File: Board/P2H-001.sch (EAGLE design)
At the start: 29 parts, among them IC1 LTC485N, IC2 74LS07N, IC3 74LS157N, IC4 LTC485N, IC5 TLC5941NT, IC6 TLC5941NT

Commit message: Tuning of routing.
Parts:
- renumbered U$1 to U1
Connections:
- net N$11 renamed LEDA
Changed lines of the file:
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@@
 <part name="SUPPLY18" library="supply2" deviceset="GND" device=""/>
 <part name="SUPPLY17" library="supply2" deviceset="VCC" device=""/>
-<part name="U$1" library="SparkFun-Boards" deviceset="ARDUINO_PRO_MINI" device=""/>
+<part name="U1" library="SparkFun-Boards" deviceset="ARDUINO_PRO_MINI" device=""/>
 </parts>
 <sheets>
@@
 <instance part="SUPPLY18" gate="GND" x="198.12" y="-68.58"/>
 <instance part="SUPPLY17" gate="G$1" x="198.12" y="-33.02"/>
-<instance part="U$1" gate="G$1" x="106.68" y="30.48"/>
+<instance part="U1" gate="G$1" x="106.68" y="30.48"/>
 </instances>
 <busses>
@@
 <wire x1="96.52" y1="38.1" x2="60.96" y2="38.1" width="0.1524" layer="91"/>
 <wire x1="60.96" y1="38.1" x2="60.96" y2="-20.32" width="0.1524" layer="91"/>
-<pinref part="U$1" gate="G$1" pin="GND"/>
+<pinref part="U1" gate="G$1" pin="GND"/>
 </segment>
 <segment>
@@
 <pinref part="SUPPLY11" gate="G$1" pin="VCC"/>
 <wire x1="124.46" y1="38.1" x2="124.46" y2="121.92" width="0.1524" layer="91"/>
-<pinref part="U$1" gate="G$1" pin="VCC"/>
+<pinref part="U1" gate="G$1" pin="VCC"/>
 </segment>
 <segment>
@@
 <wire x1="53.34" y1="45.72" x2="53.34" y2="53.34" width="0.1524" layer="91"/>
 <junction x="53.34" y="53.34"/>
-<pinref part="U$1" gate="G$1" pin="TXO"/>
+<pinref part="U1" gate="G$1" pin="TXO"/>
 </segment>
 </net>
@@
 <label x="86.36" y="22.86" size="1.778" layer="95"/>
 <label x="93.98" y="-7.62" size="1.778" layer="95"/>
-<pinref part="U$1" gate="G$1" pin="7"/>
+<pinref part="U1" gate="G$1" pin="7"/>
 </segment>
 </net>
@@
 <junction x="147.32" y="-10.16"/>
 <label x="93.98" y="-10.16" size="1.778" layer="95"/>
-<pinref part="U$1" gate="G$1" pin="*6"/>
+<pinref part="U1" gate="G$1" pin="*6"/>
 </segment>
 </net>
@@
 <label x="86.36" y="30.48" size="1.778" layer="95"/>
 <label x="93.98" y="-15.24" size="1.778" layer="95"/>
-<pinref part="U$1" gate="G$1" pin="4"/>
+<pinref part="U1" gate="G$1" pin="4"/>
 </segment>
 </net>
@@
 <wire x1="127" y1="-2.54" x2="127" y2="25.4" width="0.1524" layer="91"/>
 <wire x1="127" y1="25.4" x2="119.38" y2="25.4" width="0.1524" layer="91"/>
-<pinref part="U$1" gate="G$1" pin="13"/>
+<pinref part="U1" gate="G$1" pin="13"/>
 </segment>
 </net>
@@
 <wire x1="124.46" y1="-5.08" x2="124.46" y2="20.32" width="0.1524" layer="91"/>
 <wire x1="124.46" y1="20.32" x2="119.38" y2="20.32" width="0.1524" layer="91"/>
-<pinref part="U$1" gate="G$1" pin="*11"/>
+<pinref part="U1" gate="G$1" pin="*11"/>
 </segment>
 </net>
@@
 <pinref part="VDD2" gate="G$1" pin="VDD"/>
 <wire x1="119.38" y1="45.72" x2="119.38" y2="129.54" width="0.1524" layer="91"/>
-<pinref part="U$1" gate="G$1" pin="RAW"/>
+<pinref part="U1" gate="G$1" pin="RAW"/>
 </segment>
 <segment>
@@
 <label x="86.36" y="27.94" size="1.778" layer="95"/>
 <label x="93.98" y="-12.7" size="1.778" layer="95"/>
-<pinref part="U$1" gate="G$1" pin="*5"/>
+<pinref part="U1" gate="G$1" pin="*5"/>
 </segment>
 </net>
@@
 <label x="86.36" y="20.32" size="1.778" layer="95"/>
 <label x="93.98" y="-38.1" size="1.778" layer="95"/>
-<pinref part="U$1" gate="G$1" pin="8"/>
+<pinref part="U1" gate="G$1" pin="8"/>
 </segment>
 </net>
@@
 <wire x1="53.34" y1="-35.56" x2="53.34" y2="43.18" width="0.1524" layer="91"/>
 <wire x1="53.34" y1="43.18" x2="96.52" y2="43.18" width="0.1524" layer="91"/>
-<pinref part="U$1" gate="G$1" pin="RXI"/>
+<pinref part="U1" gate="G$1" pin="RXI"/>
 </segment>
 </net>
@@
 <label x="86.36" y="40.64" size="1.778" layer="95"/>
 <label x="45.72" y="5.08" size="1.778" layer="95"/>
-<pinref part="U$1" gate="G$1" pin="RST"/>
+<pinref part="U1" gate="G$1" pin="RST"/>
 </segment>
 </net>
@@
 <label x="86.36" y="35.56" size="1.778" layer="95"/>
 <label x="45.72" y="15.24" size="1.778" layer="95"/>
-<pinref part="U$1" gate="G$1" pin="2"/>
+<pinref part="U1" gate="G$1" pin="2"/>
 </segment>
 </net>
@@
 <label x="86.36" y="33.02" size="1.778" layer="95"/>
 <label x="45.72" y="2.54" size="1.778" layer="95"/>
-<pinref part="U$1" gate="G$1" pin="*3"/>
+<pinref part="U1" gate="G$1" pin="*3"/>
 </segment>
 </net>
@@
 <pinref part="SV2" gate="1" pin="6"/>
 <label x="93.98" y="0" size="1.778" layer="95"/>
-<pinref part="U$1" gate="G$1" pin="*9"/>
+<pinref part="U1" gate="G$1" pin="*9"/>
 </segment>
 </net>
@@
 <label x="157.48" y="15.24" size="1.778" layer="95"/>
 <label x="175.26" y="33.02" size="1.778" layer="95"/>
-<pinref part="U$1" gate="G$1" pin="A0"/>
+<pinref part="U1" gate="G$1" pin="A0"/>
 </segment>
 </net>
@@
 <pinref part="SV2" gate="1" pin="8"/>
 <label x="147.32" y="33.02" size="1.778" layer="95"/>
-<pinref part="U$1" gate="G$1" pin="A1"/>
+<pinref part="U1" gate="G$1" pin="A1"/>
 </segment>
 </net>
@@
 <label x="157.48" y="10.16" size="1.778" layer="95"/>
 <label x="175.26" y="35.56" size="1.778" layer="95"/>
-<pinref part="U$1" gate="G$1" pin="A2"/>
+<pinref part="U1" gate="G$1" pin="A2"/>
 </segment>
 </net>
@@
 <pinref part="SV2" gate="1" pin="10"/>
 <label x="147.32" y="35.56" size="1.778" layer="95"/>
-<pinref part="U$1" gate="G$1" pin="A3"/>
-</segment>
-</net>
-<net name="N$11" class="0">
+<pinref part="U1" gate="G$1" pin="A3"/>
+</segment>
+</net>
+<net name="LEDA" class="0">
 <segment>
 <pinref part="IC5" gate="G$1" pin="OUT9"/>
@@
 <wire x1="152.4" y1="45.72" x2="121.92" y2="45.72" width="0.1524" layer="91"/>
 <label x="127" y="45.72" size="1.778" layer="95"/>
-<pinref part="U$1" gate="G$1" pin="*10"/>
+<pinref part="U1" gate="G$1" pin="*10"/>
 </segment>
 </net>
@@
 <wire x1="121.92" y1="10.16" x2="121.92" y2="-17.78" width="0.1524" layer="91"/>
 <label x="93.98" y="-17.78" size="1.778" layer="95"/>
-<pinref part="U$1" gate="G$1" pin="A6"/>
+<pinref part="U1" gate="G$1" pin="A6"/>
 </segment>
 </net>
@@
 <label x="157.48" y="2.54" size="1.778" layer="95"/>
 <label x="175.26" y="38.1" size="1.778" layer="95"/>
-<pinref part="U$1" gate="G$1" pin="A4"/>
+<pinref part="U1" gate="G$1" pin="A4"/>
 </segment>
 </net>
@@
 <label x="93.98" y="5.08" size="1.778" layer="95"/>
 <label x="147.32" y="38.1" size="1.778" layer="95"/>
-<pinref part="U$1" gate="G$1" pin="A5"/>
+<pinref part="U1" gate="G$1" pin="A5"/>
 </segment>
 </net>
@@
 <wire x1="193.04" y1="-43.18" x2="205.74" y2="-43.18" width="0.1524" layer="91"/>
 <label x="157.48" y="12.7" size="1.778" layer="95"/>
-<pinref part="U$1" gate="G$1" pin="A7"/>
-</segment>
-</net>
+<pinref part="U1" gate="G$1" pin="A7"/>
+</segment>
+</net>

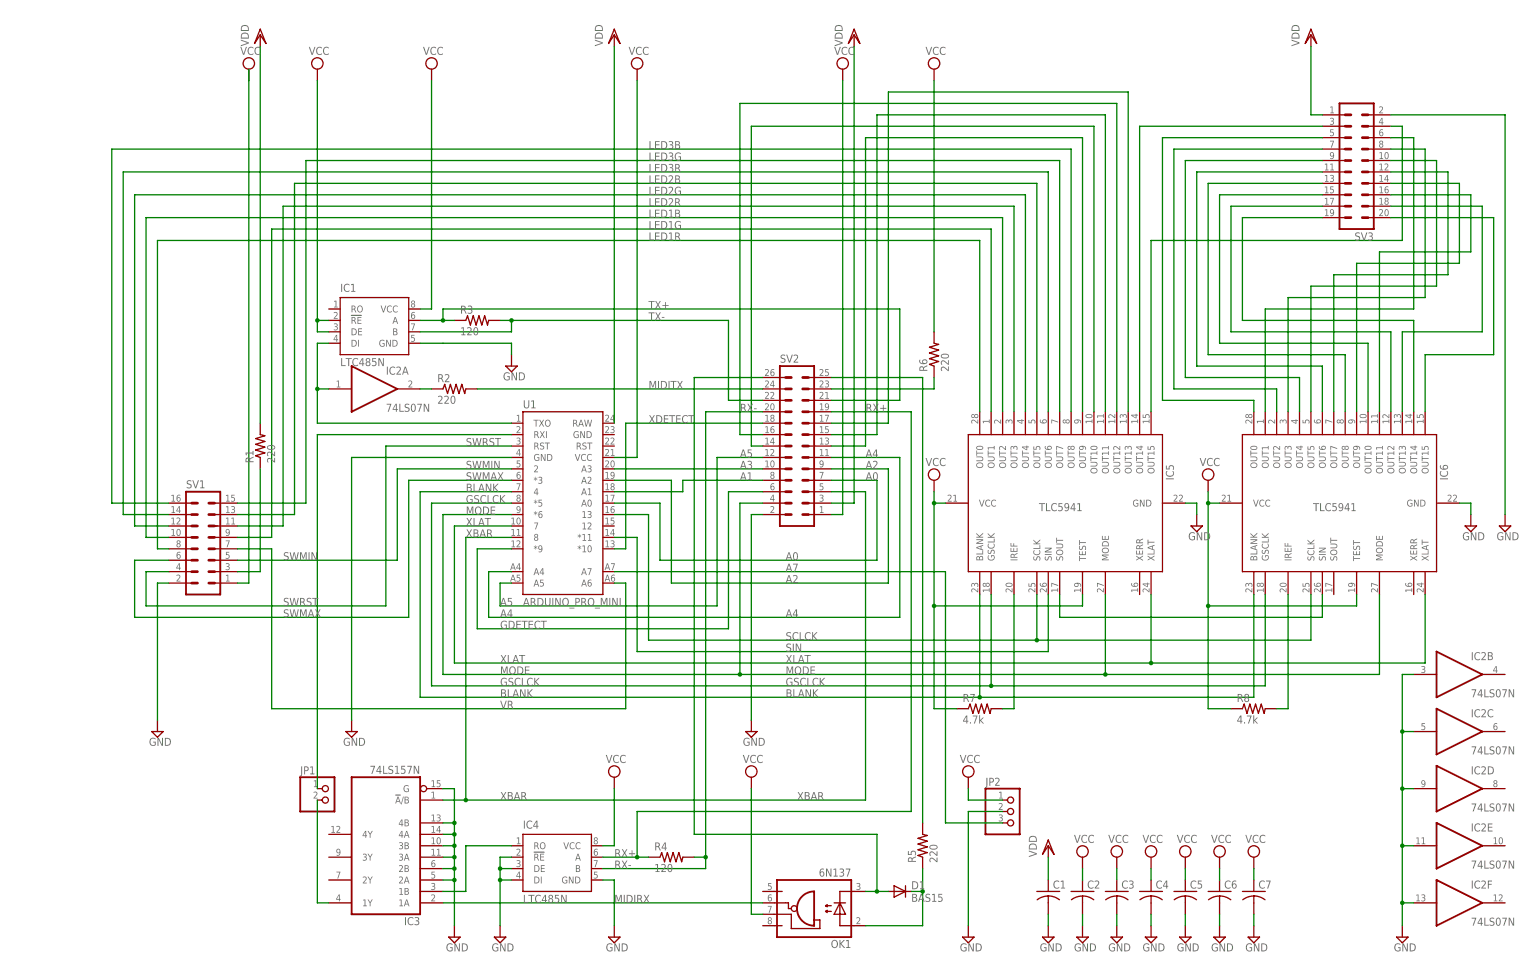
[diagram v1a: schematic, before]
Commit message: Now MIDI IN has detector connector.
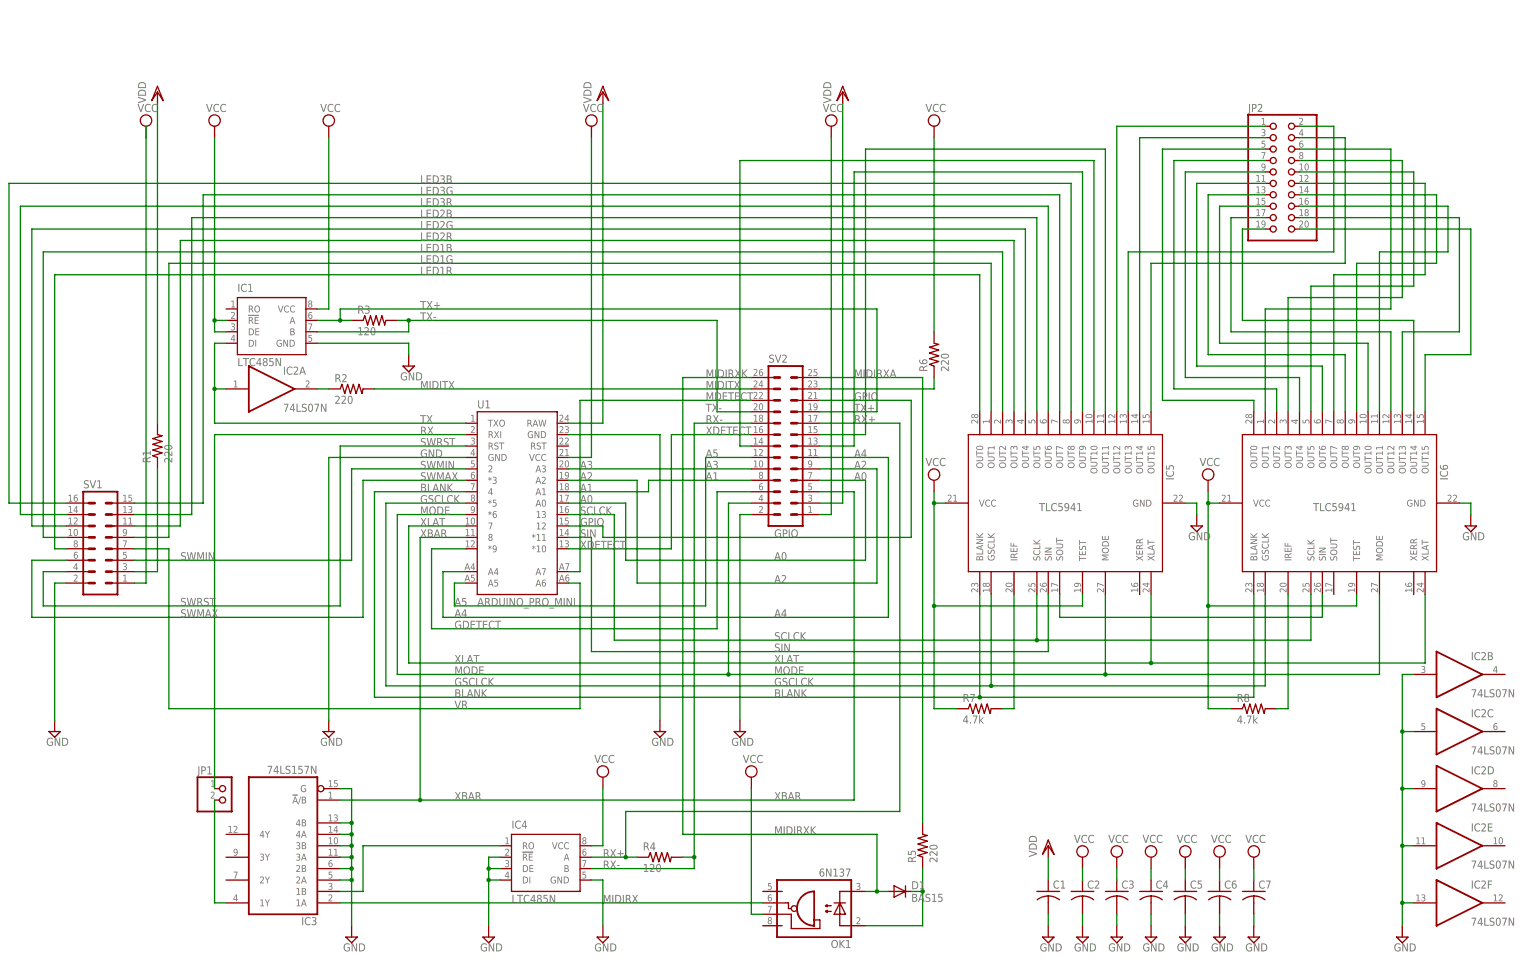
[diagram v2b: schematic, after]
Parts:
- removed SV3: (no value), con-ml:ML20L
- JP2: device pinhead:PINHD-1X3 -> pinhead:PINHD-2X10
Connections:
- net N$18 renamed MIDIRXA
- net N$20 renamed MIDIRXK
- removed net A7: JP2.3, U1.A7
- removed net N$21: IC5.OUT12, SV2.16
- removed net N$22: IC5.OUT13, SV2.17
- new net GPIO: SV2.21, U1.12
- new net MDETECT: SV2.22, U1.A7
- new net N$3: IC5.OUT12, JP2.1
- new net N$5: IC5.OUT13, JP2.2
- net GND: now also U1.GND@2; no longer JP2.2, SV3.2
- net N$24: now also JP2.3; no longer SV3.3
- net N$25: now also JP2.4; no longer SV3.4
- net N$26: now also JP2.5; no longer SV3.5
- net N$27: now also JP2.7; no longer SV3.7
- net N$28: now also JP2.9; no longer SV3.9
- net N$29: now also JP2.11; no longer SV3.11
- net N$30: now also JP2.13; no longer SV3.13
- net N$31: now also JP2.15; no longer SV3.15
- net N$32: now also JP2.17; no longer SV3.17
- net N$33: now also JP2.19; no longer SV3.19
- net N$34: now also JP2.6; no longer SV3.6
- net N$35: now also JP2.8; no longer SV3.8
- net N$36: now also JP2.10; no longer SV3.10
- net N$39: now also JP2.12; no longer SV3.12
- net N$40: now also JP2.14; no longer SV3.14
- net N$41: now also JP2.16; no longer SV3.16
- net N$42: now also JP2.18; no longer SV3.18
- net N$43: now also JP2.20; no longer SV3.20
- net RX+: now also SV2.17; no longer SV2.19
- net RX-: now also SV2.18; no longer SV2.20
- net TX+: now also SV2.19; no longer SV2.21
- net TX-: now also SV2.20; no longer SV2.22
- net VCC: no longer JP2.1
- net VDD: no longer SV3.1
- net XDETECT: now also SV2.16; no longer SV2.18
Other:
- moved on the sheet: IC1, IC2A, IC3, IC4, JP1, R1, R2, R3, R4, SV1, SV2, U1

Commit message: Now frontport is PH connector.
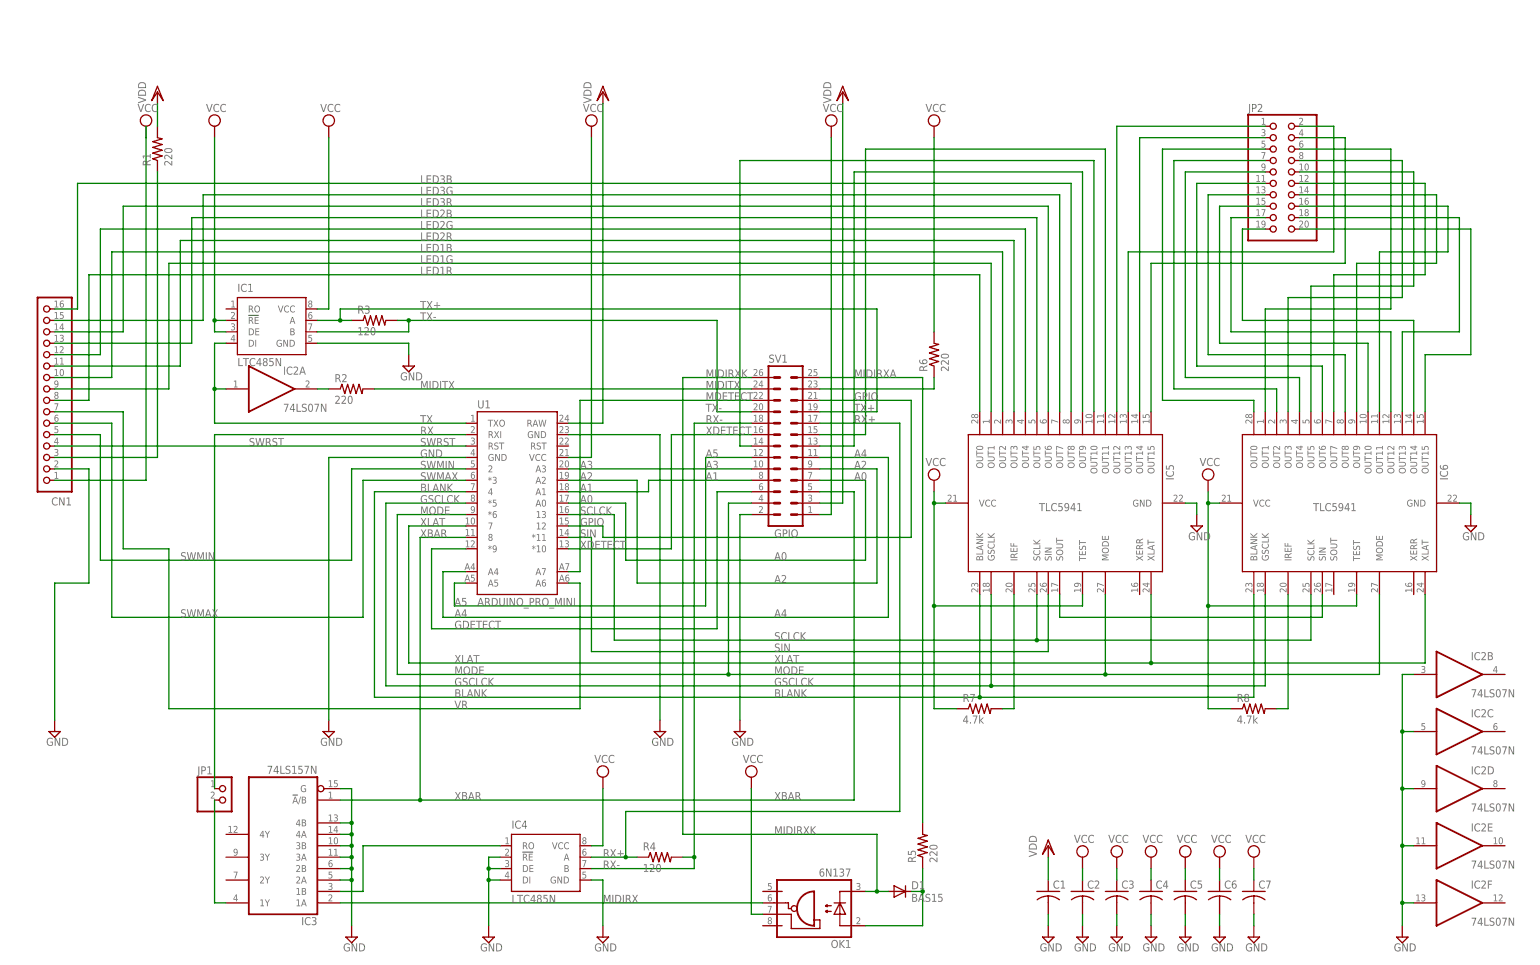
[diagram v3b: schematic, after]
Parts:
- removed SV2: (no value), con-ml:ML26L
- added CN1: (no value), jst-ph:S16B-PH-K-S
- SV1: device con-ml:ML16L -> con-ml:ML26L
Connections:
- net A0: now also SV1.7; no longer SV2.7
- net A1: now also SV1.8; no longer SV2.8
- net A2: now also SV1.9; no longer SV2.9
- net A3: now also SV1.10; no longer SV2.10
- net A4: now also SV1.11; no longer SV2.11
- net A5: now also SV1.12; no longer SV2.12
- net GDETECT: now also SV1.6; no longer SV2.6
- net GND: now also CN1.2; no longer SV2.2
- net GPIO: now also SV1.21; no longer SV2.21
- net LED1B: now also CN1.10; no longer SV1.10
- net LED1G: now also CN1.9; no longer SV1.9
- net LED1R: now also CN1.8; no longer SV1.8
- net LED2B: now also CN1.13; no longer SV1.13
- net LED2G: now also CN1.12; no longer SV1.12
- net LED2R: now also CN1.11; no longer SV1.11
- net LED3B: now also CN1.16; no longer SV1.16
- net LED3G: now also CN1.15; no longer SV1.15
- net LED3R: now also CN1.14; no longer SV1.14
- net LEDA: now also SV1.13; no longer SV2.13
- net MDETECT: now also SV1.22; no longer SV2.22
- net MIDIRXA: now also SV1.25; no longer SV2.25
- net MIDIRXK: now also SV1.26; no longer SV2.26
- net MIDITX: now also SV1.24; no longer SV2.24
- net MODE: now also SV1.4; no longer SV2.4
- net N$12: now also SV1.14; no longer SV2.14
- net N$14: now also SV1.15; no longer SV2.15
- net N$4: now also SV1.23; no longer SV2.23
- net N$7: now also CN1.3; no longer SV1.3
- net RX+: now also SV1.17; no longer SV2.17
- net RX-: now also SV1.18; no longer SV2.18
- net SWMAX: now also CN1.6; no longer SV1.6
- net SWMIN: now also CN1.5; no longer SV1.5
- net SWRST: now also CN1.4; no longer SV1.4
- net TX+: now also SV1.19; no longer SV2.19
- net TX-: now also SV1.20; no longer SV2.20
- net VCC: now also CN1.1; no longer SV2.1
- net VDD: now also SV1.3; no longer SV2.3
- net VR: now also CN1.7; no longer SV1.7
- net XBAR: now also SV1.5; no longer SV2.5
- net XDETECT: now also SV1.16; no longer SV2.16
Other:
- moved on the sheet: R1
